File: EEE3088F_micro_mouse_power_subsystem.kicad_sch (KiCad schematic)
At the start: 17 parts, among them J1 Conn_02x16_Odd_Even, J2 Conn_01x02, U1 INA219AIDCNR, U2 DRV8833PWPR, U3 DRV8833PWPR, U4 TPTLV70033DDCR

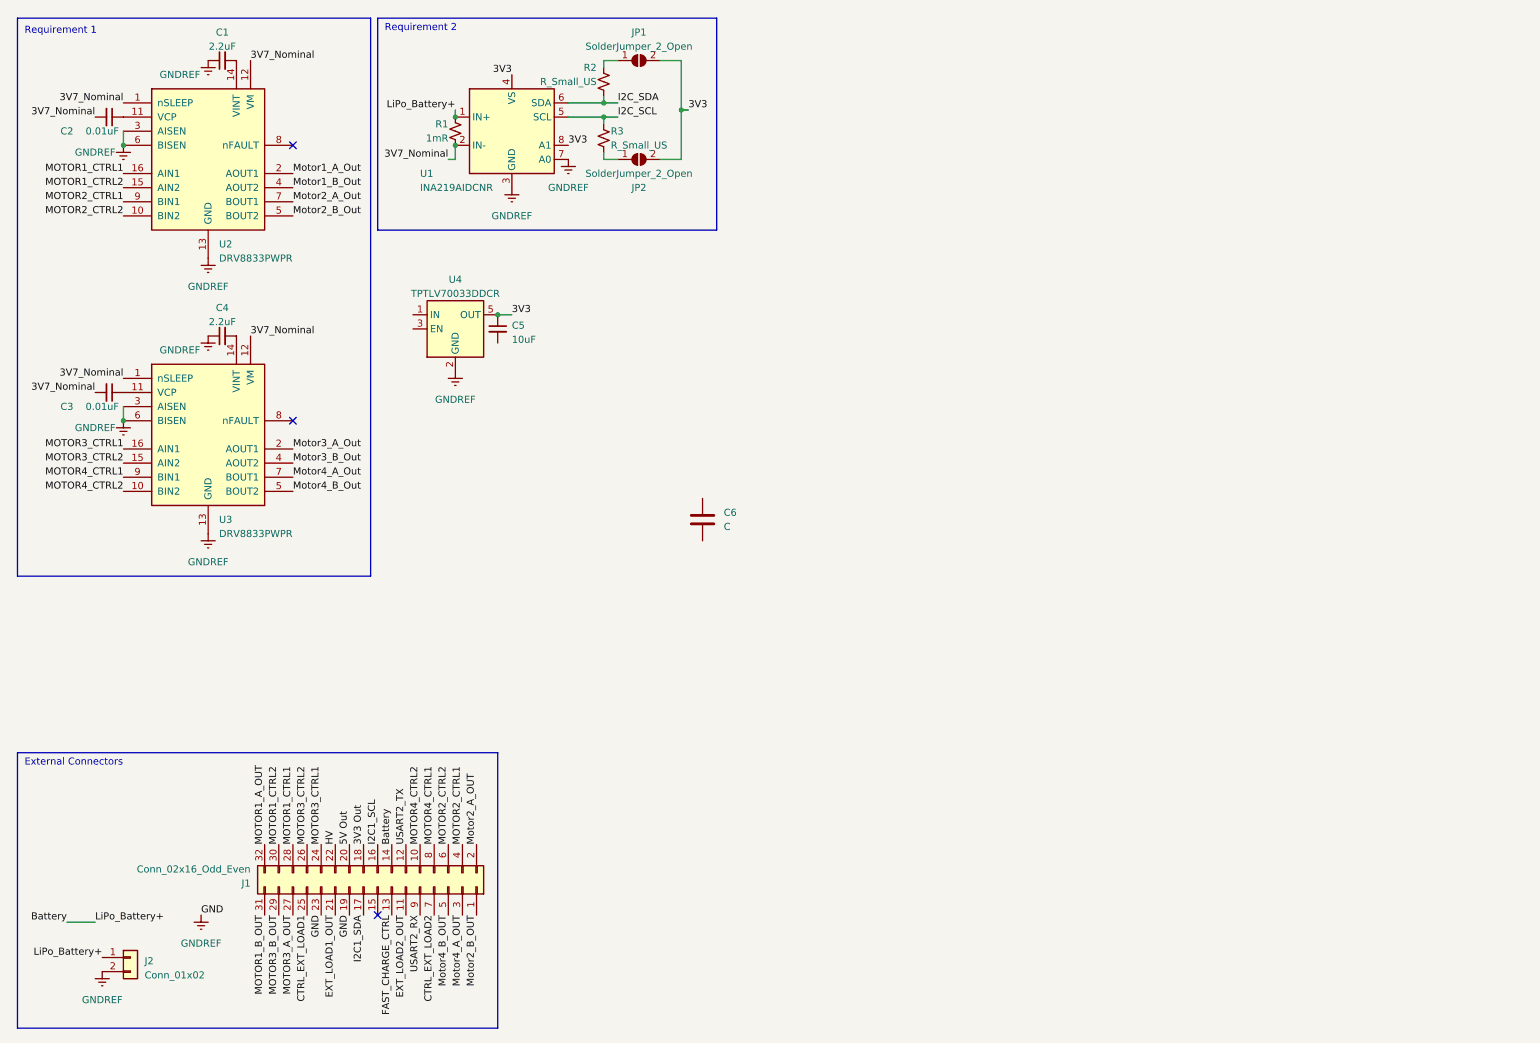
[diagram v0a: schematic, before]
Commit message: Battery charging circuitry added
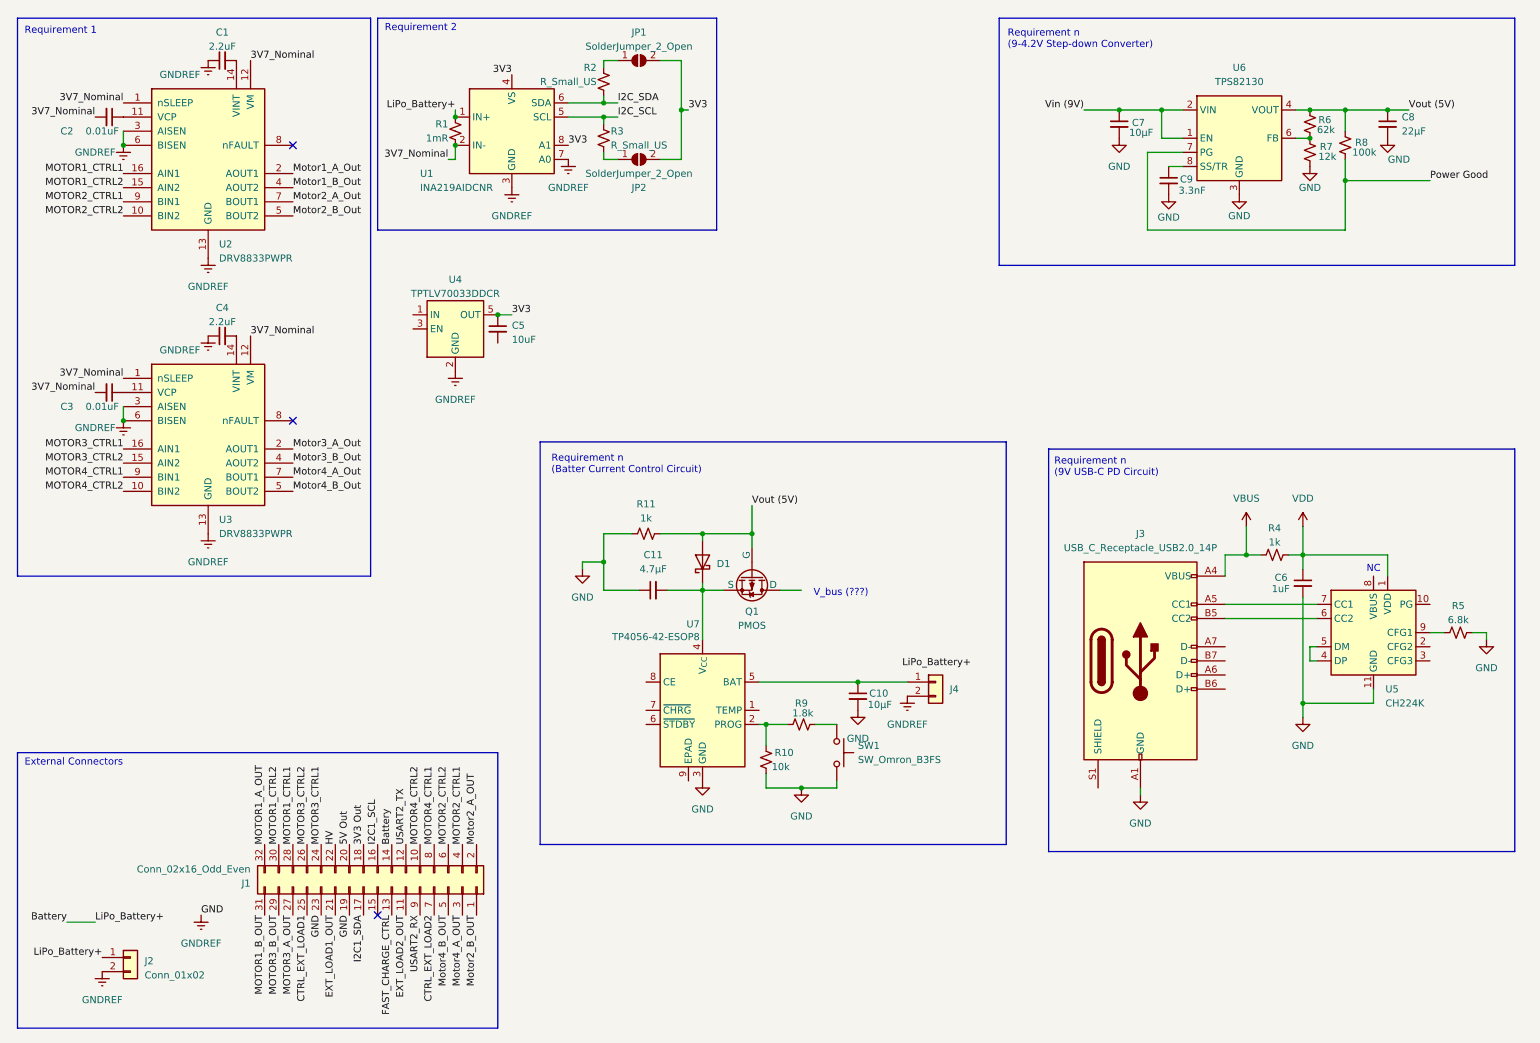
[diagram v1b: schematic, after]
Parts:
- removed C6: C, symbol Device:C
- added C10, C7: 10µF, symbol Device:C_Small
- added C11: 4.7µF, symbol Device:C_Small
- added C6: 1uF, symbol Device:C_Small
- added C8: 22µF, symbol Device:C_Small
- added C9: 3.3nF, symbol Device:C_Small
- added D1: D_Schottky, symbol Device:D_Schottky
- added J3: USB_C_Receptacle_USB2.0_14P, symbol Connector:USB_C_Receptacle_USB2.0_14P
- added J4: Conn_01x02, symbol Connector_Generic:Conn_01x02
- added Q1: PMOS, symbol Simulation_SPICE:PMOS
- added R10: 10k, symbol Device:R_Small_US
- added R11, R4: 1k, symbol Device:R_Small_US
- added R5: 6.8k, symbol Device:R_Small_US
- added R6: 62k, symbol Device:R_Small_US
- added R7: 12k, symbol Device:R_Small_US
- added R8: 100k, symbol Device:R_Small_US
- added R9: 1.8k, symbol Device:R_Small_US
- added SW1: SW_Omron_B3FS, symbol Switch:SW_Omron_B3FS
- added U5: CH224K, Package_SO:SSOP-10-1EP_3.9x4.9mm_P1mm_EP2.1x3.3mm, symbol Interface_USB:CH224K
- added U6: TPS82130, Package_LGA:Texas_SIL0008D_MicroSiP-8-1EP_2.8x3mm_P0.65mm_EP1.1x1.9mm_ThermalVias, symbol Regulator_Switching:TPS82130
- added U7: TP4056-42-ESOP8, Package_SO:SOIC-8-1EP_3.9x4.9mm_P1.27mm_EP2.41x3.3mm_ThermalVias, symbol Battery_Management:TP4056-42-ESOP8
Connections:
- net GNDREF renamed GND
- net GND: now also C10.2, C11.1, C6.2, C7.2, C8.2, C9.2, J3.A1 (GND), J3.A12 (GND), J3.B1 (GND), J3.B12 (GND), J4.2 (Pin_2), R10.1, R11.1, R5.2, R7.2, SW1.2, U5.11 (GND), U6.3 (GND), U6.9 (GND), U7.3 (GND)
- new net: R10.2, R9.1, U7.2 (PROG)
- new net: R9.2, SW1.1
- new net: J3.A5 (CC1), U5.7 (CC1)
- new net: J3.B5 (CC2), U5.6 (CC2)
- new net: U5.4 (DP), U5.5 (DM)
- new net: R5.1, U5.9 (CFG1)
- new net: C11.2, D1.1 (K), Q1.3 (S), U7.4 (V_{CC})
- new net: C10.1, J4.1 (Pin_1), U7.5 (BAT)
- new net: R6.2, R7.1, U6.6 (FB)
- new net: C9.1, U6.8 (SS/TR)
- new net Power Good: R8.2, U6.7 (PG)
- new net VBUS: J3.A4 (VBUS), J3.A9 (VBUS), J3.B4 (VBUS), J3.B9 (VBUS), R4.2
- new net VDD: C6.1, R4.1, U5.1 (VDD)
- new net Vin (9V): C7.1, U6.1 (EN), U6.2 (VIN)
- new net Vout (5V): C8.1, D1.2 (A), Q1.2 (G), R11.2, R6.1, R8.1, U6.4 (VOUT), U6.5 (VOUT)
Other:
- note added: "NC"
- note added: "Requirement n (9-4.2V Step-down Converter)"
- note added: "Requirement n (9V USB-C PD Circuit)"
- note added: "Requirement n (Batter Current Control Circuit)"
- note added: "V_bus (???)"

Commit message: Added circuits for requirements 7 and 8
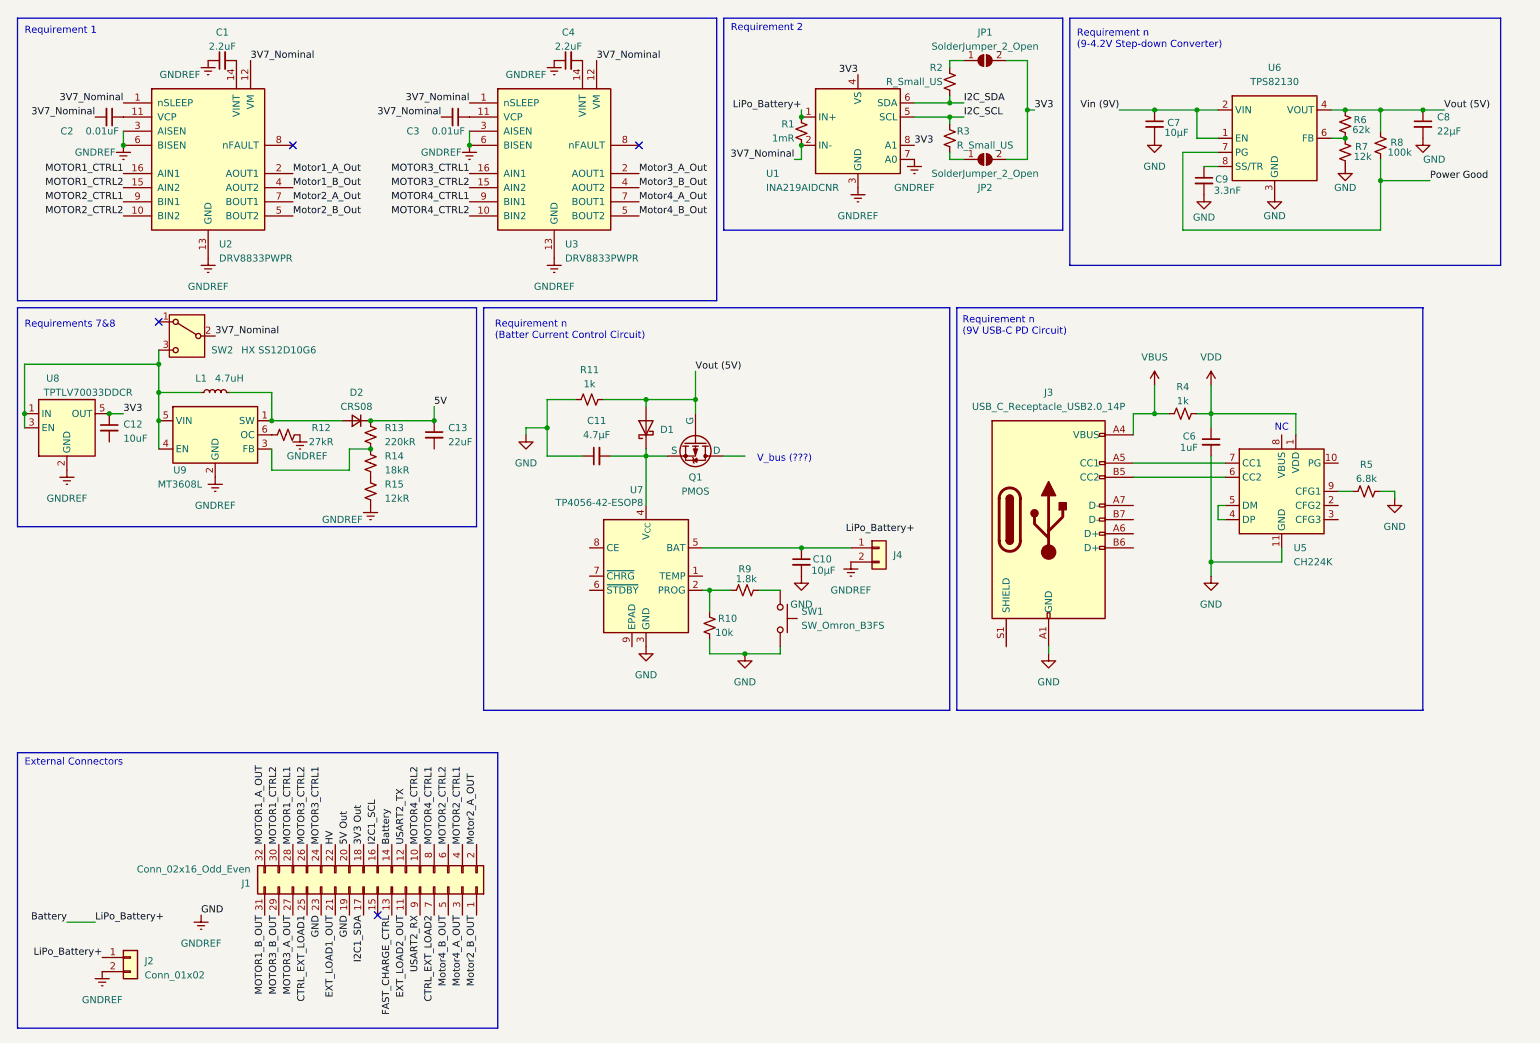
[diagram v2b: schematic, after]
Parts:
- removed C5: 10uF, symbol Device:C_Small
- removed U4: TPTLV70033DDCR, Package_TO_SOT_SMD:SOT-23-5, symbol Regulator_Linear:TPS78233DDC
- added C12: 10uF, symbol Device:C_Small
- added C13: 22uF, symbol Device:C_Small
- added D2: CRS08, symbol Device:D_Small
- added L1: 4.7uH, symbol Device:L_Small
- added R12: 27kR, symbol Device:R_Small_US
- added R13: 220kR, symbol Device:R_Small_US
- added R14: 18kR, symbol Device:R_Small_US
- added R15: 12kR, symbol Device:R_Small_US
- added SW2: HX SS12D10G6, symbol Switch:SW_SPDT
- added U8: TPTLV70033DDCR, Package_TO_SOT_SMD:SOT-23-5, symbol Regulator_Linear:TPS78233DDC
- added U9: MT3608L, Package_TO_SOT_SMD:SOT-23-6, symbol Regulator_Switching:AP3211K
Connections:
- net 3V3: now also C12.1, U8.5 (OUT)
- net 3V7_Nominal: now also SW2.2 (B)
- net GND: now also R12.2, R15.2, U8.2 (GND), U8.4 (GND), U9.2 (GND)
- new net: R13.2, R14.1, U9.3 (FB)
- new net: R14.2, R15.1
- new net: D2.2 (A), L1.2, U9.1 (SW)
- new net: L1.1, SW2.3 (C), U8.1 (IN), U8.3 (EN), U9.4 (EN), U9.5 (VIN)
- new net: R12.1, U9.6 (OC)
- new net 5V: C13.1, D2.1 (K), R13.1
- no-connect marks 3 -> 4
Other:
- note added: "Requirements 7&8"
- moved on the sheet: C10, C11, C3, C4, C6, C7, C8, C9, D1, J3, J4, JP1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

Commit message: Minor updates after meeting
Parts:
- removed J2: Conn_01x02, symbol Connector_Generic:Conn_01x02
- C10: value 10µF -> 22µF
- renumbered J4 to J2
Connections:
- net 3V3 is gone; now on net 3V3 Out: C12.1, JP1.2 (B), JP2.2 (B), U1.4 (VS), U1.8 (A1), U8.5 (OUT)
- net 5V is gone; now on net 5V Out: C13.1, D2.1 (K), R13.1
- net GND: no longer C1.1, C4.1, J2.2 (Pin_2), R12.2, R15.2, U1.3 (GND), U1.7 (A0), U2.13 (GND), U2.3 (AISEN), U2.6 (BISEN), U3.13 (GND), U3.3 (AISEN), U3.6 (BISEN), U8.2 (GND), U8.4 (GND), U9.2 (GND)
- new net GNDREF: C1.1, C4.1, J2.2 (Pin_2), R12.2, R15.2, U1.3 (GND), U1.7 (A0), U2.13 (GND), U2.3 (AISEN), U2.6 (BISEN), U3.13 (GND), U3.3 (AISEN), U3.6 (BISEN), U8.2 (GND), U8.4 (GND), U9.2 (GND)
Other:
- moved on the sheet: C7, C8, C9, J1, JP1, JP2, R1, R2, R3, R6, R7, R8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
